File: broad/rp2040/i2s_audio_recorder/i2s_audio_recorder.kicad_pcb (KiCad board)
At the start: 2 copper layers, 55 parts, among them J1 USB_C_Receptacle_USB2.0_16P, J2 Conn_01x04_Pin, J3 SD_Card_Device, J4 Conn_01x08_Pin, J5 Conn_01x08_Pin, J6 Conn_01x08_Pin, SW1 TS342A2P-WZ, SW2 TS342A2P-WZ, SW3 TS342A2P-WZ, SW4 TS342A2P-WZ, U1 SMBJ5.0CA, U2 RP2040, U3 SMBJ5.0CA, U4 SMBJ5.0CA, U5 AMS1117-3.3, U6 MSM261S4030H0R, U7 W25Q128JVS, Y1 12M

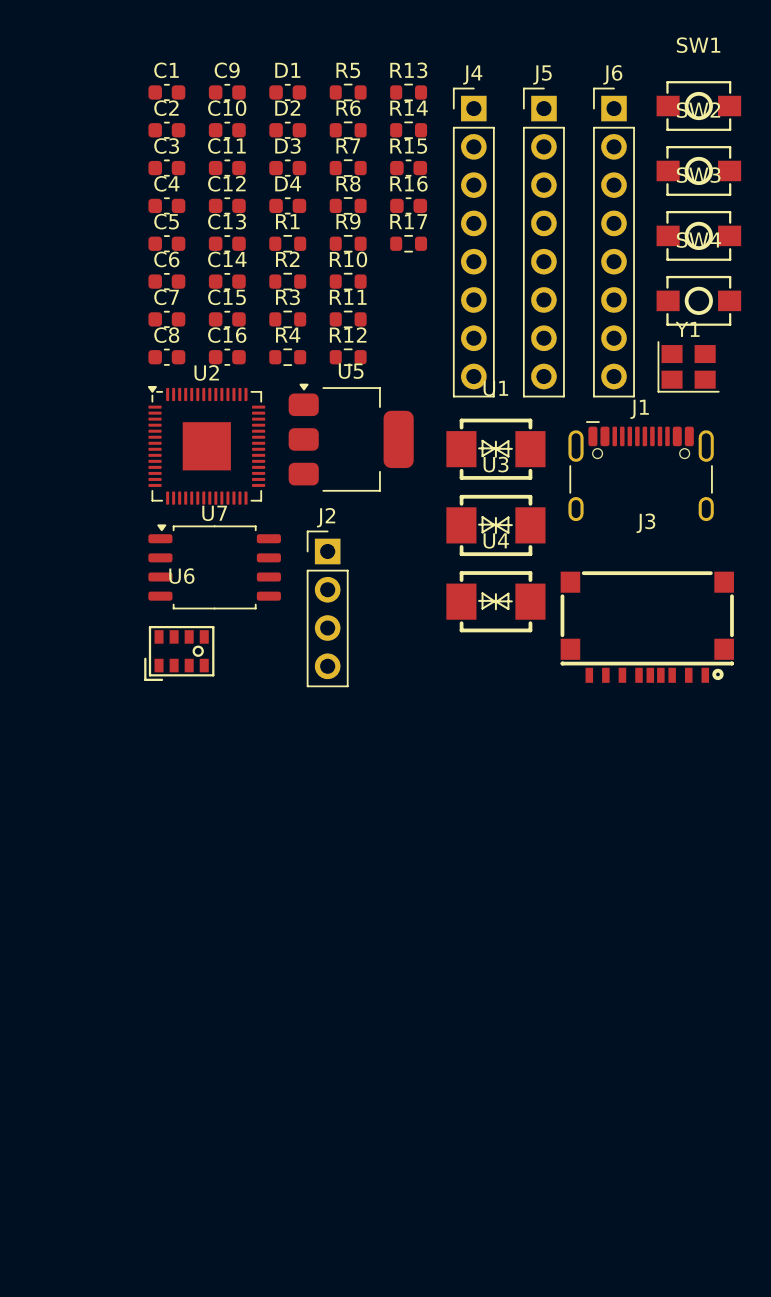
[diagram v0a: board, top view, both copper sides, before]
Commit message: Finish basic layout of `i2s_audio_recorder`
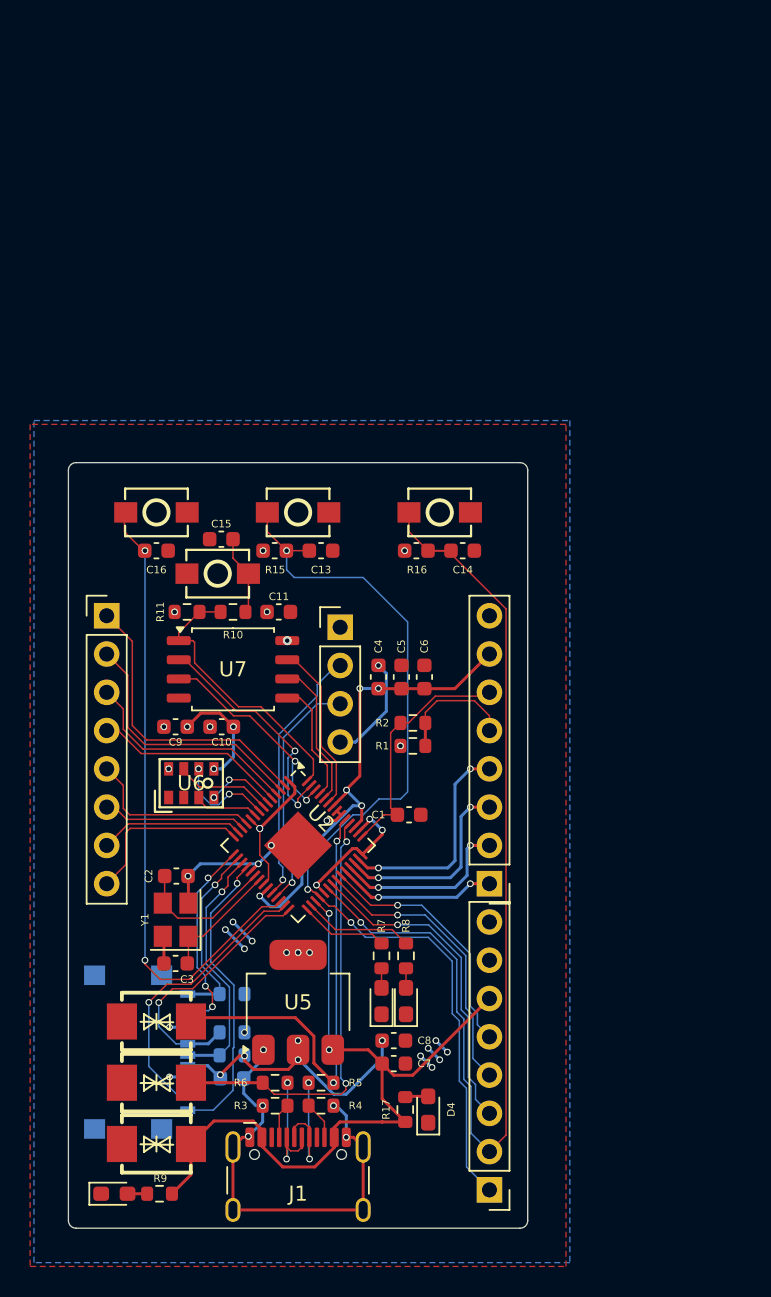
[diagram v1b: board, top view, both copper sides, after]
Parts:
- removed SW1, SW2, SW3, SW4: TS342A2P-WZ, easyeda2kicad:SW-SMD_L4.0-W2.9-LS5.0
- added BOOT1: TS342A2P-WZ, easyeda2kicad:SW-SMD_L4.0-W2.9-LS5.0, F.Cu at (135.0, 74.3)
- added G***: LOGO, LOGO, B.Cu at (151.8, 70.8)
- added RUN1: TS342A2P-WZ, easyeda2kicad:SW-SMD_L4.0-W2.9-LS5.0, F.Cu at (131.0, 70.2)
- added START1: TS342A2P-WZ, easyeda2kicad:SW-SMD_L4.0-W2.9-LS5.0, F.Cu at (149.7, 70.2)
- added STOP1: TS342A2P-WZ, easyeda2kicad:SW-SMD_L4.0-W2.9-LS5.0, F.Cu at (140.4, 70.2)
- added kibuzzard-66D862BB: G***, kibuzzard-66D862BB, B.Cu at (131.0, 77.1)
- added kibuzzard-66D86311: G***, kibuzzard-66D86311, B.Cu at (149.7, 77.1)
- added kibuzzard-66D86311: G***, kibuzzard-66D86311, B.Cu at (149.7, 97.4)
- added kibuzzard-66D8638E: G***, kibuzzard-66D8638E, B.Cu at (130.9, 79.6)
- added kibuzzard-66D86392: G***, kibuzzard-66D86392, B.Cu at (131.0, 82.2)
- added kibuzzard-66D86398: G***, kibuzzard-66D86398, B.Cu at (130.9, 84.7)
- added kibuzzard-66D863A8: G***, kibuzzard-66D863A8, B.Cu at (131.0, 87.3)
- added kibuzzard-66D863AE: G***, kibuzzard-66D863AE, B.Cu at (130.9, 89.8)
- added kibuzzard-66D863B6: G***, kibuzzard-66D863B6, B.Cu at (131.3, 92.3)
- added kibuzzard-66D863CD: G***, kibuzzard-66D863CD, B.Cu at (131.3, 94.9)
- added kibuzzard-66D863EF: G***, kibuzzard-66D863EF, B.Cu at (149.4, 79.6)
- added kibuzzard-66D86401: G***, kibuzzard-66D86401, B.Cu at (148.1, 82.2)
- added kibuzzard-66D86417: G***, kibuzzard-66D86417, B.Cu at (148.1, 84.7)
- added kibuzzard-66D86448: G***, kibuzzard-66D86448, B.Cu at (149.4, 100.0)
- added kibuzzard-66D86450: G***, kibuzzard-66D86450, B.Cu at (149.4, 102.5)
- added kibuzzard-66D86456: G***, kibuzzard-66D86456, B.Cu at (149.4, 105.0)
- added kibuzzard-66D8645B: G***, kibuzzard-66D8645B, B.Cu at (149.4, 107.6)
- added kibuzzard-66D86461: G***, kibuzzard-66D86461, B.Cu at (149.4, 110.1)
- added kibuzzard-66D86466: G***, kibuzzard-66D86466, B.Cu at (149.5, 112.7)
- added kibuzzard-66D8646D: G***, kibuzzard-66D8646D, B.Cu at (149.4, 115.2)
- added kibuzzard-66D864FE: G***, kibuzzard-66D864FE, B.Cu at (149.2, 87.3)
- added kibuzzard-66D8650E: G***, kibuzzard-66D8650E, B.Cu at (149.2, 89.8)
- added kibuzzard-66D86516: G***, kibuzzard-66D86516, B.Cu at (149.2, 92.3)
- added kibuzzard-66D8651F: G***, kibuzzard-66D8651F, B.Cu at (149.2, 94.9)
- added kibuzzard-66D86547: G***, kibuzzard-66D86547, B.Cu at (145.9, 94.9)
- added kibuzzard-66D86585: G***, kibuzzard-66D86585, B.Cu at (145.9, 92.3)
- added kibuzzard-66D86595: G***, kibuzzard-66D86595, B.Cu at (145.9, 89.8)
- added kibuzzard-66D865A1: G***, kibuzzard-66D865A1, B.Cu at (145.9, 87.3)
- C12, J3, R12, R13, R14: moved to B.Cu
- D1, D2, D3, D4: footprint Capacitor_SMD:C_0603_1608Metric -> LED_SMD:LED_0603_1608Metric_Pad1.05x0.95mm_HandSolder
- moved J5 71.8 mm to (153.1, 115.2), turned to 180 degrees
- moved D3 69.0 mm to (128.2, 115.5)
- moved R5 65.7 mm to (141.9, 108.1)
- moved R9 64.3 mm to (131.2, 115.5), turned to 180 degrees
- moved R13 63.5 mm to (136.0, 104.7)
- moved R6 63.4 mm to (138.8, 108.1), turned to 180 degrees
- moved D4 60.7 mm to (149.0, 109.9), turned to 90 degrees
- moved D1 60.6 mm to (145.9, 102.7), turned to 90 degrees
- moved R14 58.5 mm to (136.0, 102.2), turned to 180 degrees
- moved D2 58.3 mm to (147.5, 102.7), turned to 90 degrees
- moved C12 57.9 mm to (136.0, 107.8)
- moved R17 57.5 mm to (147.5, 109.9), turned to 90 degrees
- moved C3 52.8 mm to (132.2, 100.2)
- moved R7 52.3 mm to (145.9, 99.7), turned to -90 degrees
- moved R3 52.2 mm to (138.8, 109.6), turned to 180 degrees
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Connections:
- J5 pad 6: +5V -> VBUS
- J6 pad 5: +1V1 -> /ADC_VERF
- J6 pad 6: /ADC_VERF -> /ADC_AVDD
- J6 pad 7: /ADC_AVDD -> +1V1
- U2 pad 27: /SD_CMD -> /SD_CLK
- U2 pad 28: /SD_CLK -> /SD_CMD
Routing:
- net /KEY1: track 0.00 -> 72.0 mm, vias 0 -> 1
- net /KEY0: track 0.00 -> 64.8 mm, vias 0 -> 3
- net GND: track 0.00 -> 64.6 mm, vias 0 -> 25
- net VBUS: track 0.00 -> 49.9 mm, vias 0 -> 2
- net /RUN: track 0.00 -> 42.1 mm, vias 0 -> 2
- net +3V3: track 0.00 -> 39.0 mm, vias 0 -> 23
- net +1V1: track 0.00 -> 32.9 mm, vias 0 -> 5
- net /DP: track 0.00 -> 30.2 mm, vias 0 -> 2
- net /DM: track 0.00 -> 28.9 mm, vias 0 -> 2
- net /GPIO23: track 0.00 -> 21.7 mm, vias 0 -> 1
- net /SD_DAT4: track 0.00 -> 19.9 mm, vias 0 -> 1
- net /GPIO0: track 0.00 -> 19.8 mm
- net /SD_CLK: track 0.00 -> 19.3 mm, vias 0 -> 1
- net /GPIO24: track 0.00 -> 19.2 mm, vias 0 -> 1
- net /QSPI_SS: track 0.00 -> 18.5 mm
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- added copper zone on B.Cu, net +3V3
- added copper zone on F.Cu, net GND
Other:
- board outline added: 30.5 x 50.8 mm

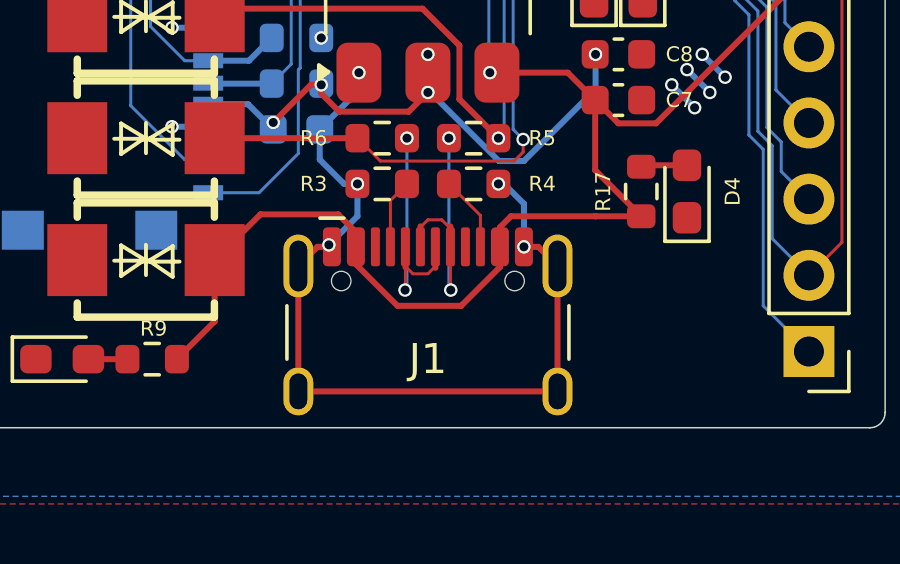
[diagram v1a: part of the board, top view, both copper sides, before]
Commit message: Add JLC code to broad
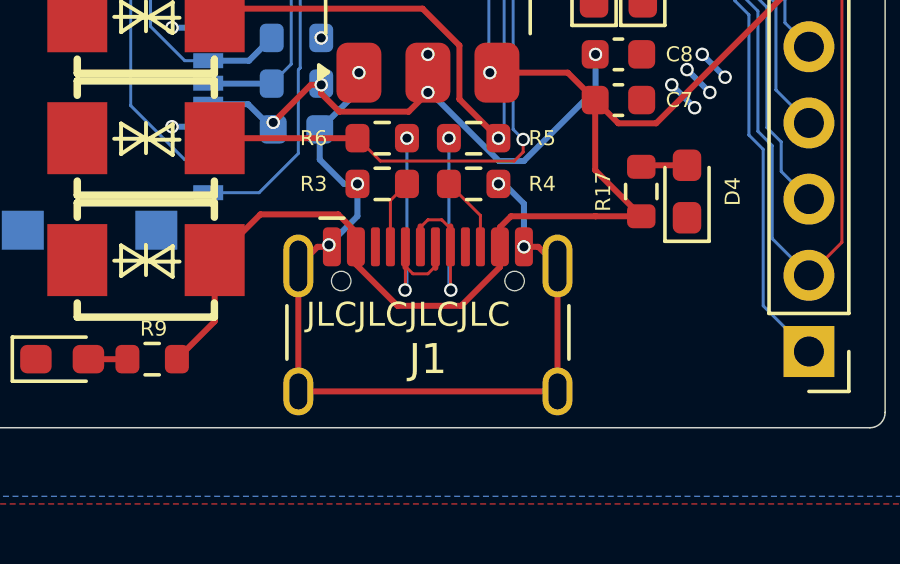
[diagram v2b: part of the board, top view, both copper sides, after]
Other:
- board text added: "JLCJLCJLCJLC"

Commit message: Change `i2s_audio_recorder` R3 R4 from `512 ohm` to `5.1k ohm`
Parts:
- R3, R4: value 512ohm -> 5.1kohm

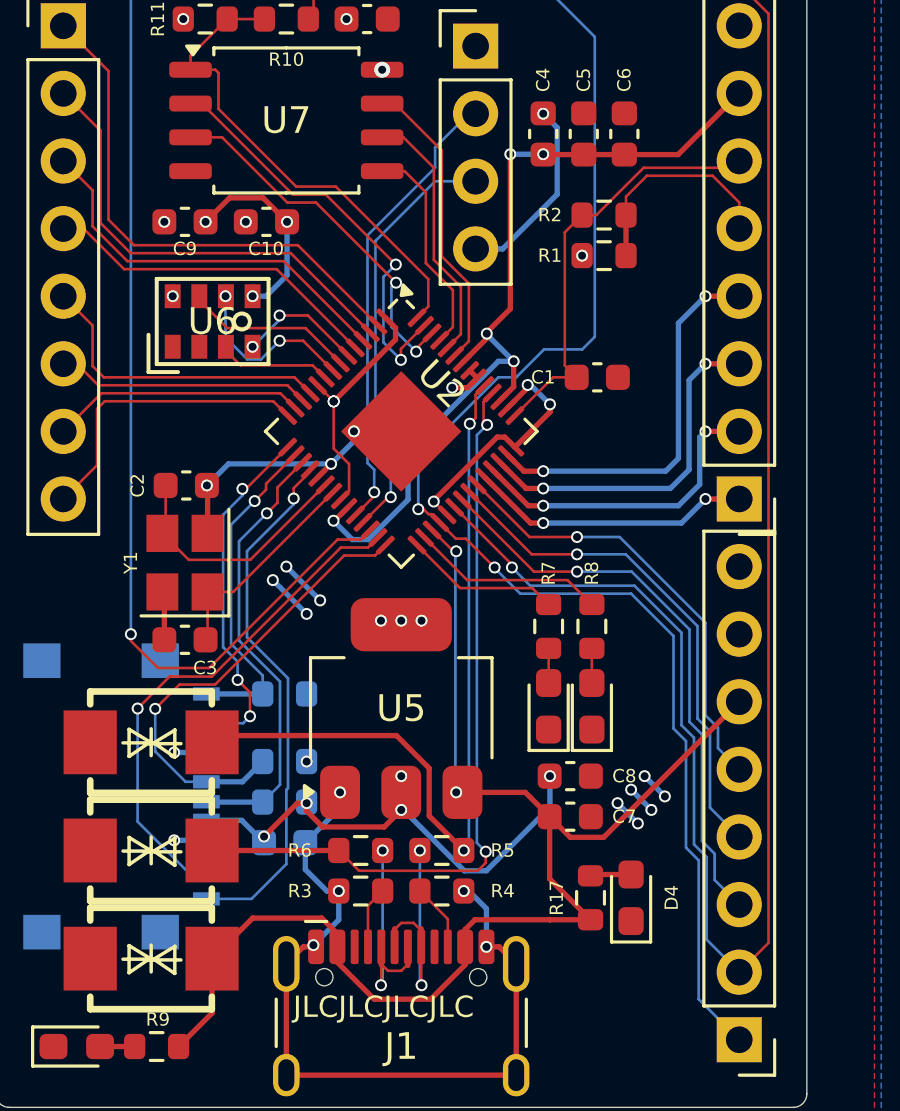
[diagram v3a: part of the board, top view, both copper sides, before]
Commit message: Re-layout of the TVS position of `i2s_audio_recorder`
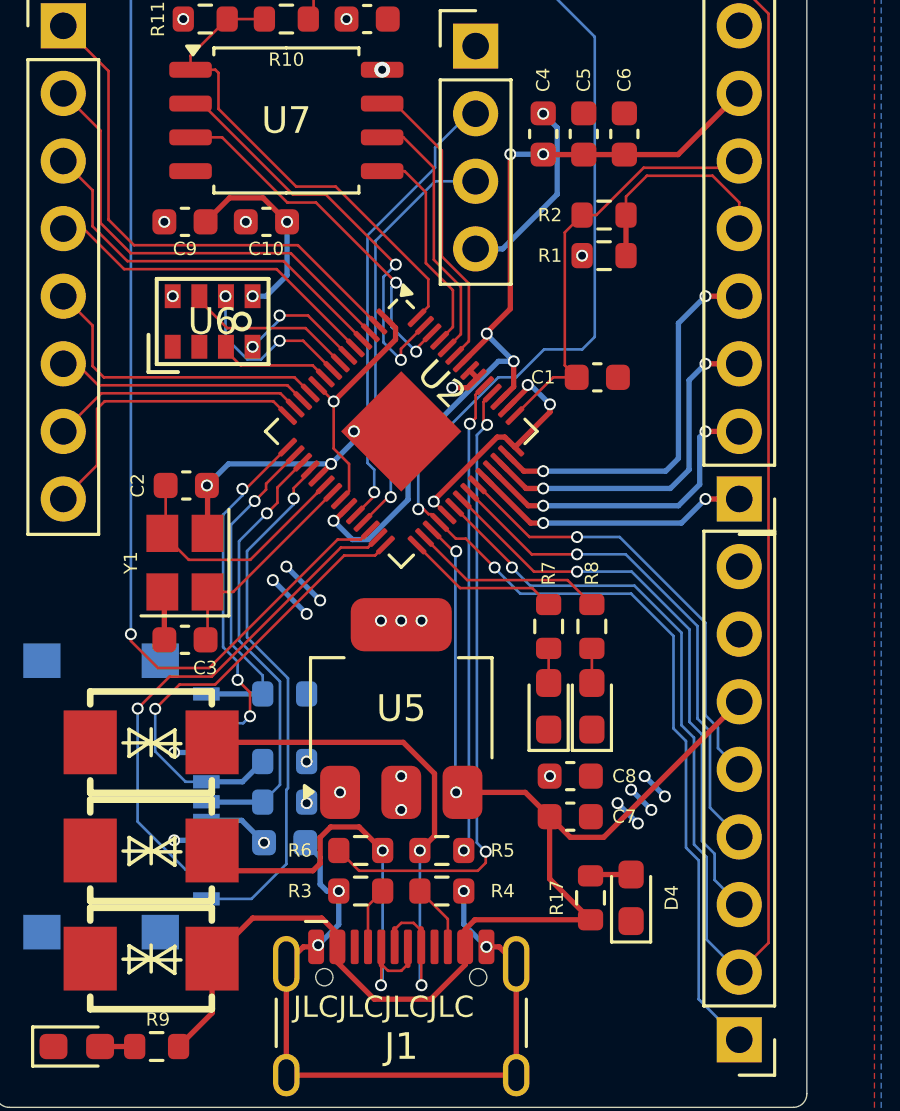
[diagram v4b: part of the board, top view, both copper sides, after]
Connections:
- U1 pad 1: /DP -> Net-(J1-D+-PadA6)
- U3 pad 1: /DM -> Net-(J1-D--PadA7)
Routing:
- net +3V3: track 39.0 -> 22.6 mm, vias 23 -> 22
- net /DP: track 30.2 -> 17.8 mm
- net Net-(J1-D+-PadA6): track 10.4 -> 22.3 mm
- net Net-(J1-D--PadA7): track 10.4 -> 18.8 mm
- net /DM: track 28.9 -> 24.1 mm
- net GND: track 64.6 -> 61.6 mm, vias 25 -> 24
